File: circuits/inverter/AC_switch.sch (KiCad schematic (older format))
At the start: 0 parts

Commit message: Add more circuitry, add library content
AC current measurement
AC filter
AC switch
DC booster
DC input
Analog frontend
drivers
inverter
main controller
power supply

new components for:
standard library (e.g. relay)
AC current sensor acs722
voltage regulator LM317L

Footprints for:
AC relay
TO-220
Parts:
- added C?: 22µ/35V, symbol Capacitor
- added D? (x4): Diode, symbol Diode
- added D? (x4): Zener, symbol Zener
- added K? (x8): OJE-SH-112HM, symbol Relay
- added L?: 1mH/500mA, symbol Inductor
- added MB?: AC_N, symbol Plated_hole
- added MB?: AC_L, symbol Plated_hole
- added Q? (x5): BSS138, symbol NMOS
- added Q?: SI4401, symbol PMOS_SO08
- added R? (x7): 1k, symbol Resistor
- added R?: 10k, symbol Resistor
- added R? (x4): 10, symbol Resistor
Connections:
- net labels added: +15V, AC_Grid_Vtg_L, AC_Grid_Vtg_N, AC_Inverter_Vtg_L, AC_Inverter_Vtg_N, AC_Relay_Vtg_L, AC_Relay_Vtg_N, GND, Grid_Relay_Ctrl, Inv_Relay_Ctrl, Relay_Ctrl_Vtg, Relay_Voltage_Ctrl
- wire segments 0 -> 86

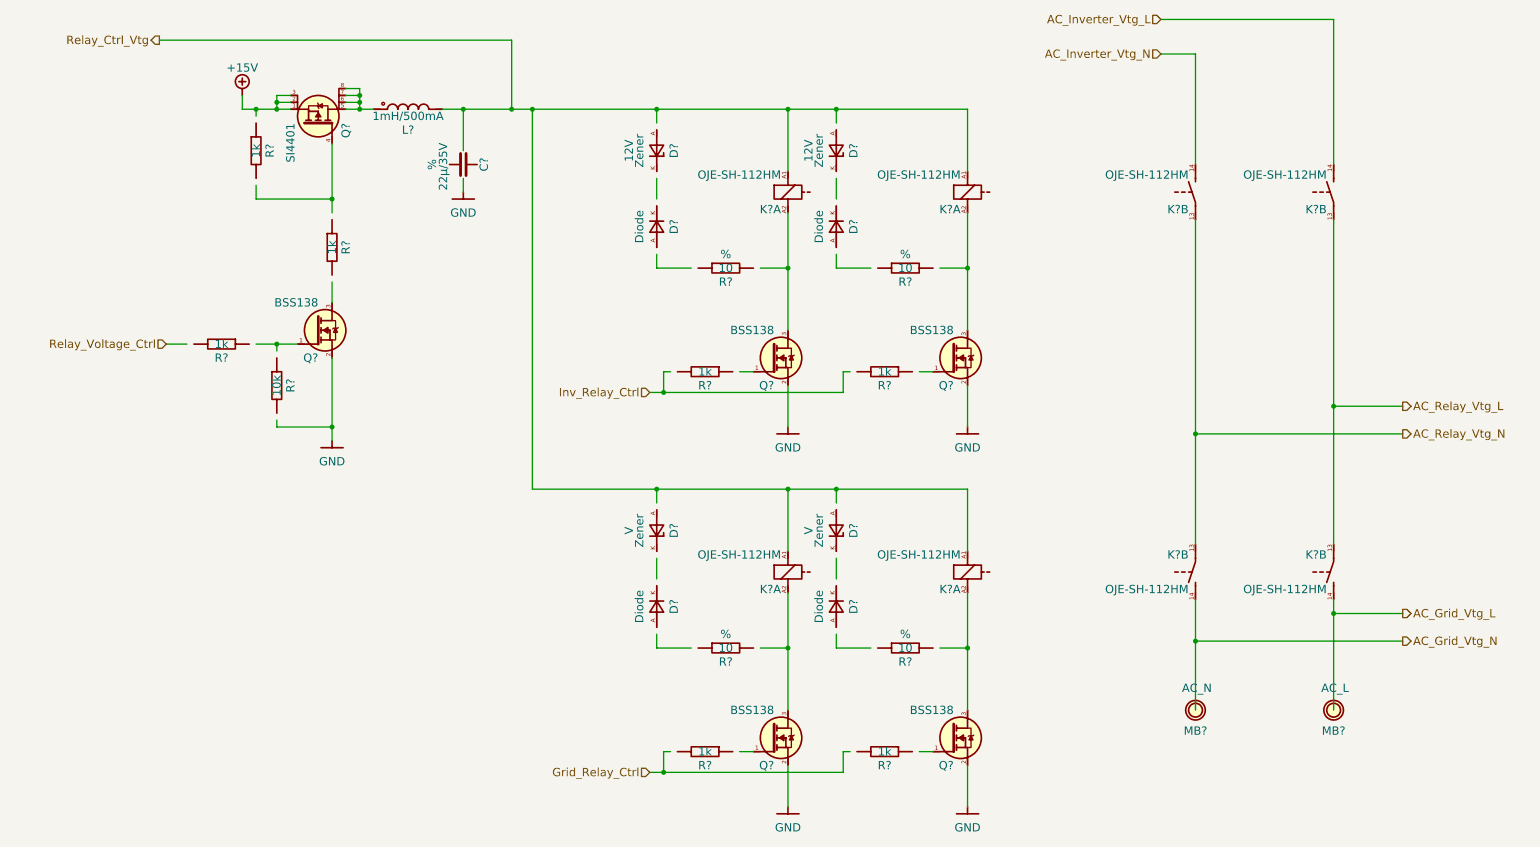
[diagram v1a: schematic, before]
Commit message: Updates all schematic pages to current components
all components are replaced with the current component library parts
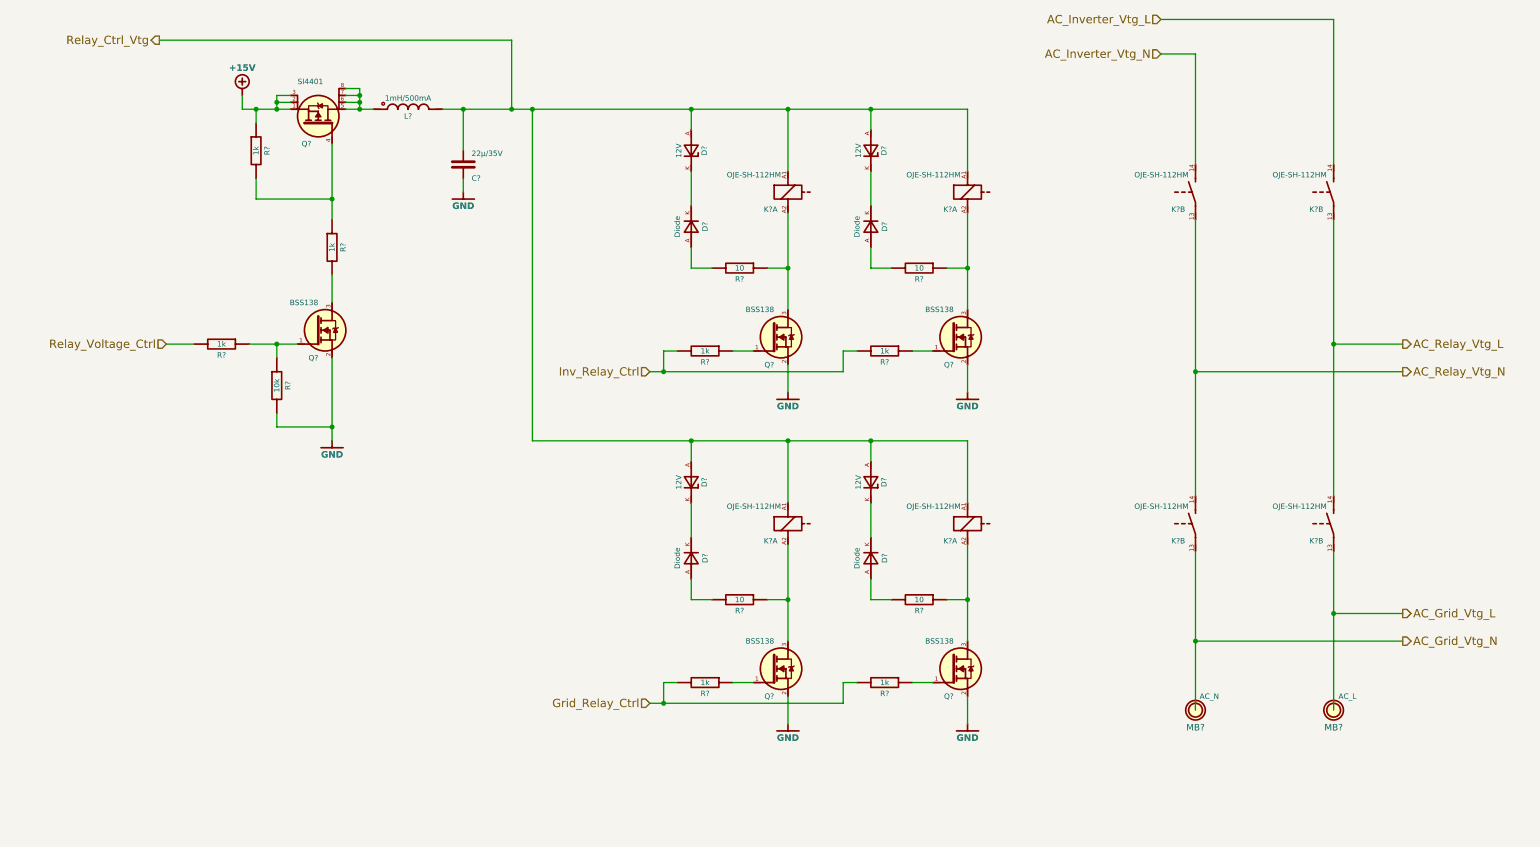
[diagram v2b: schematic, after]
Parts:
- removed C?: 22µ/35V, symbol Capacitor
- removed D? (x4): Diode, symbol Diode
- removed D? (x4): Zener, symbol Zener
- removed K? (x8): OJE-SH-112HM, symbol Relay
- removed L?: 1mH/500mA, symbol Inductor
- removed MB?: AC_N, symbol Plated_hole
- removed MB?: AC_L, symbol Plated_hole
- removed Q? (x5): BSS138, symbol NMOS
- removed Q?: SI4401, symbol PMOS_SO08
- removed R? (x7): 1k, symbol Resistor
- removed R?: 10k, symbol Resistor
- removed R? (x4): 10, symbol Resistor
- added C?: 22µ/35V, symbol Capacitor
- added D? (x4): 12V, symbol Zener
- added D? (x4): Diode, symbol Diode
- added K? (x8): OJE-SH-112HM, symbol Relay
- added L?: 1mH/500mA, symbol Inductor
- added MB?: AC_N, symbol Plated_hole
- added MB?: AC_L, symbol Plated_hole
- added Q?: SI4401, symbol PMOS_SO08
- added Q? (x5): BSS138, symbol NMOS
- added R? (x7): 1k, symbol Resistor
- added R?: 10k, symbol Resistor
- added R? (x4): 10, symbol Resistor
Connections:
- wire segments 86 -> 114

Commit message: bulk-updates libraries and schematics
schematic is updated to Kicad 5.1.14
updates various sheets with new circuits
adds various component libraries
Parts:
- added D?: Diode, symbol OSSI_standard_components:Diode
- C?: symbol Capacitor -> OSSI_standard_components:Capacitor
- D? (x4): symbol Zener -> OSSI_standard_components:Zener
- D? (x4): symbol Diode -> OSSI_standard_components:Diode
- K? (x8): symbol Relay -> OSSI_standard_components:Relay
- L?: symbol Inductor -> OSSI_standard_components:Inductor
- MB? (x2): symbol Plated_hole -> OSSI_standard_components:Plated_hole
- Q?: symbol PMOS_SO08 -> OSSI_standard_components:PMOS_SO08
- Q? (x5): symbol NMOS -> OSSI_standard_components:NMOS
- R? (x12): symbol Resistor -> OSSI_standard_components:Resistor
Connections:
- net +15V: now reaches Q?.1 (S), Q?.2 (S), Q?.3 (S), R?.1
- net GND: now reaches Q?.2 (S), R?.2
- net GND: now also C?.1, Q?.2 (S), Q?.2 (S), Q?.2 (S), Q?.2 (S), D?.A
- net at L?.1, Q?.5 (D), Q?.6 (D)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: now also D?.K
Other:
- note added: "720 Ω coil resistance\n→ 12 V÷720 Ω≈17 mA"
- moved on the sheet: C?, L?
